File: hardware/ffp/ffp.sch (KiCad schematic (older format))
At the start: 17 parts, among them IC1 STM32F042K6T7, IC2 MCP1700, IC3 MIC2004-0_5YM5, J2 USB4085, J3 PROG, P1 SWD_TC

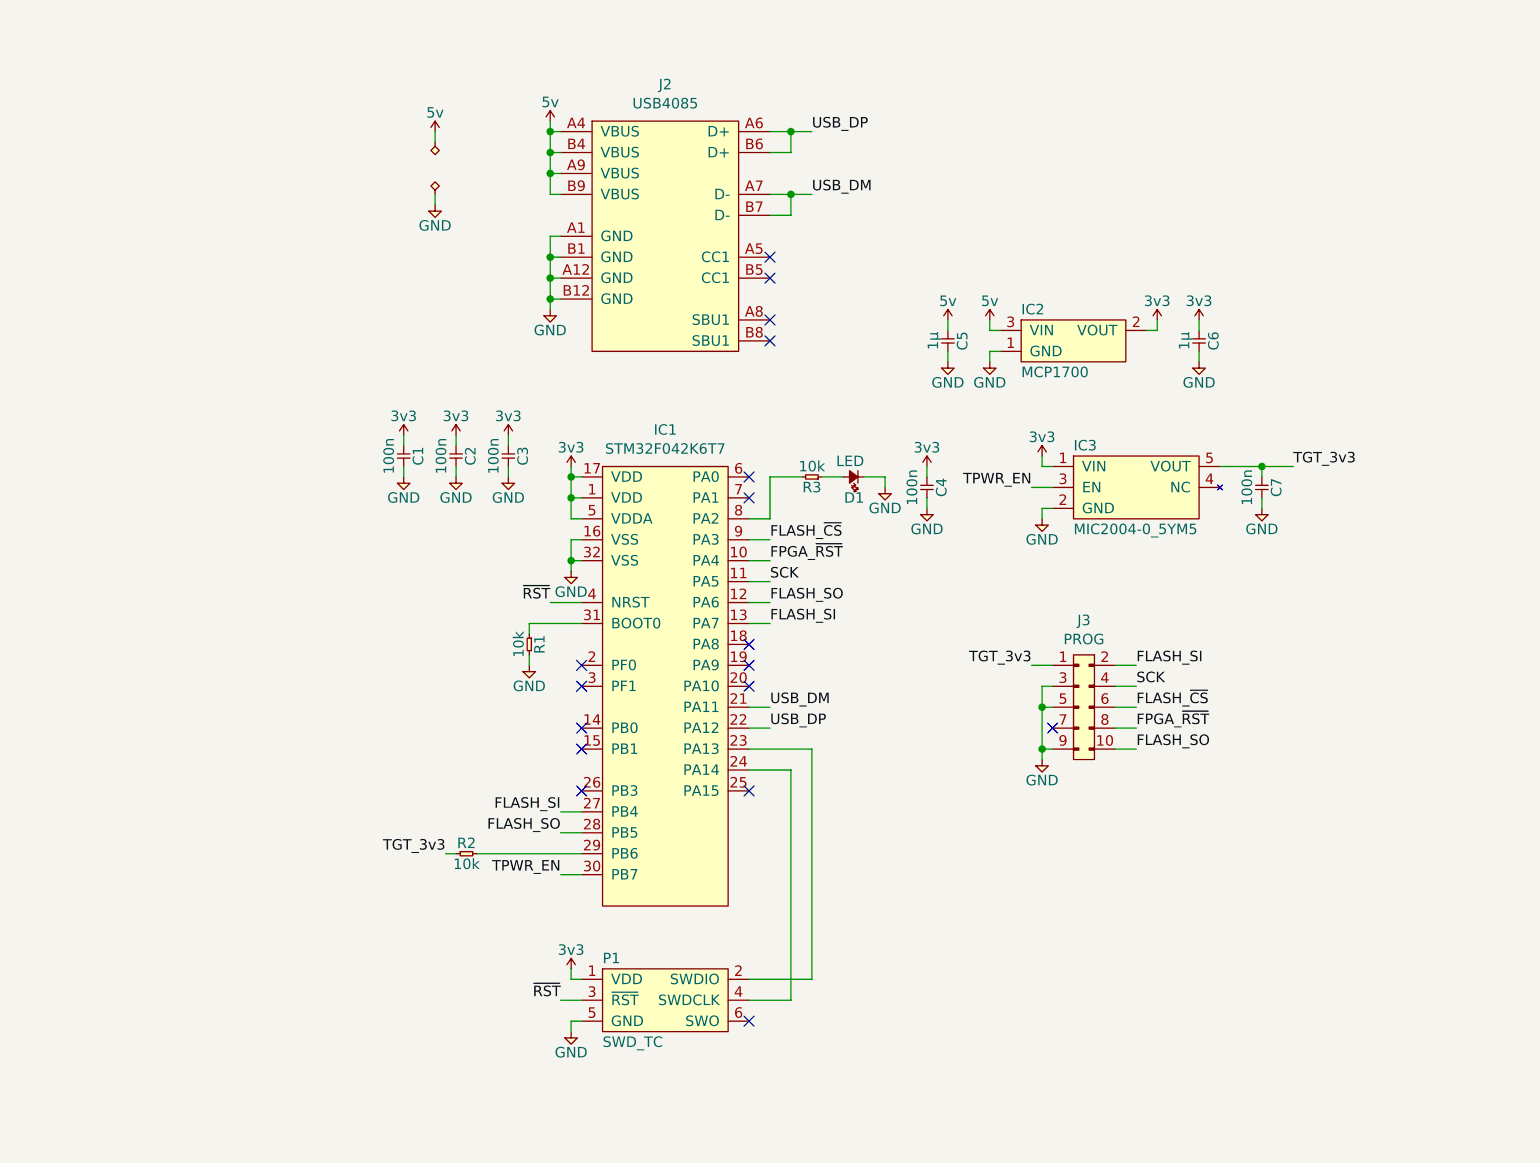
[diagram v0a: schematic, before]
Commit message: Tidy schematic and render PDF
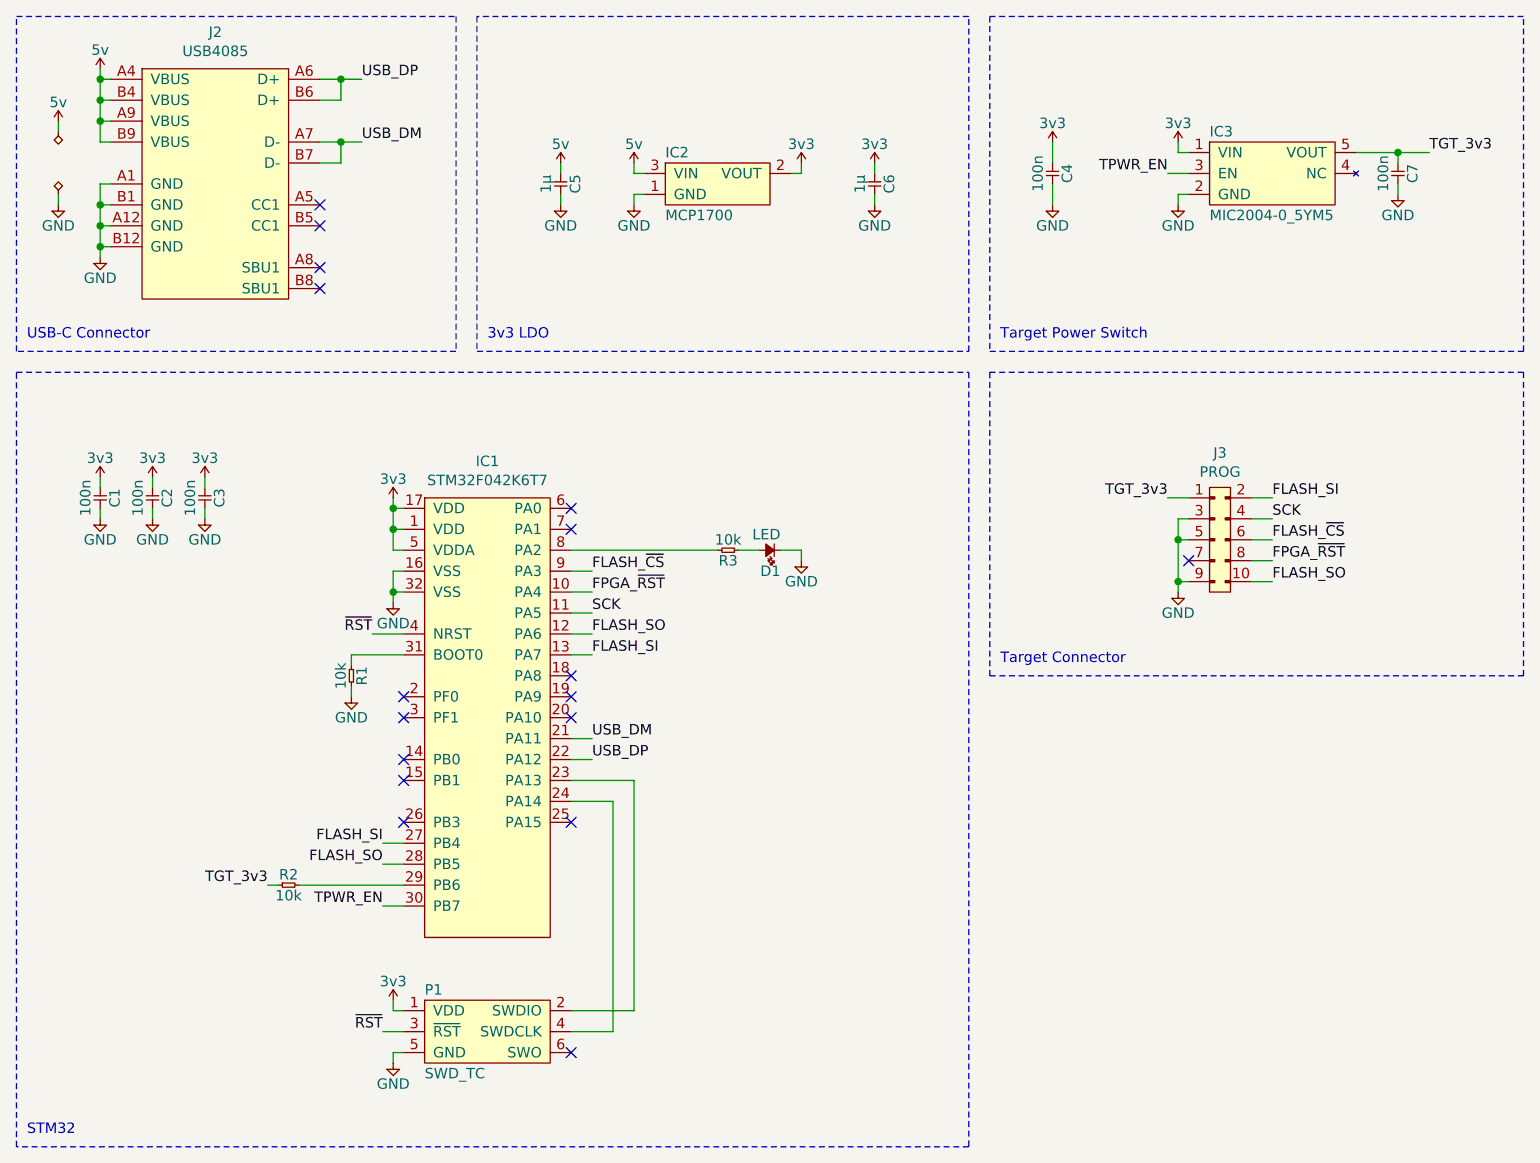
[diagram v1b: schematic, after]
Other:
- note added: "3v3 LDO"
- note added: "STM32"
- note added: "Target Connector"
- note added: "Target Power Switch"
- note added: "USB-C Connector"
- moved on the sheet: C1, C2, C3, C4, C5, C6, C7, D1, IC1, IC2, IC3, J2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
